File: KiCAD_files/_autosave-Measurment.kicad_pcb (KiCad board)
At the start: 2 copper layers, 90 x 63 mm, 66 parts, among them J1 Measurment_stage_outline_outp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, J2 Measurment_stage_outline_sign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, J3 Conn_01x02, U1 NMA1505SC, U2 AMC1100, U3 AMC1100, U4 AMC1311, U5 R-78C5.0-1.0, U6 AMS1117-3.3, U7 NMA1505SC

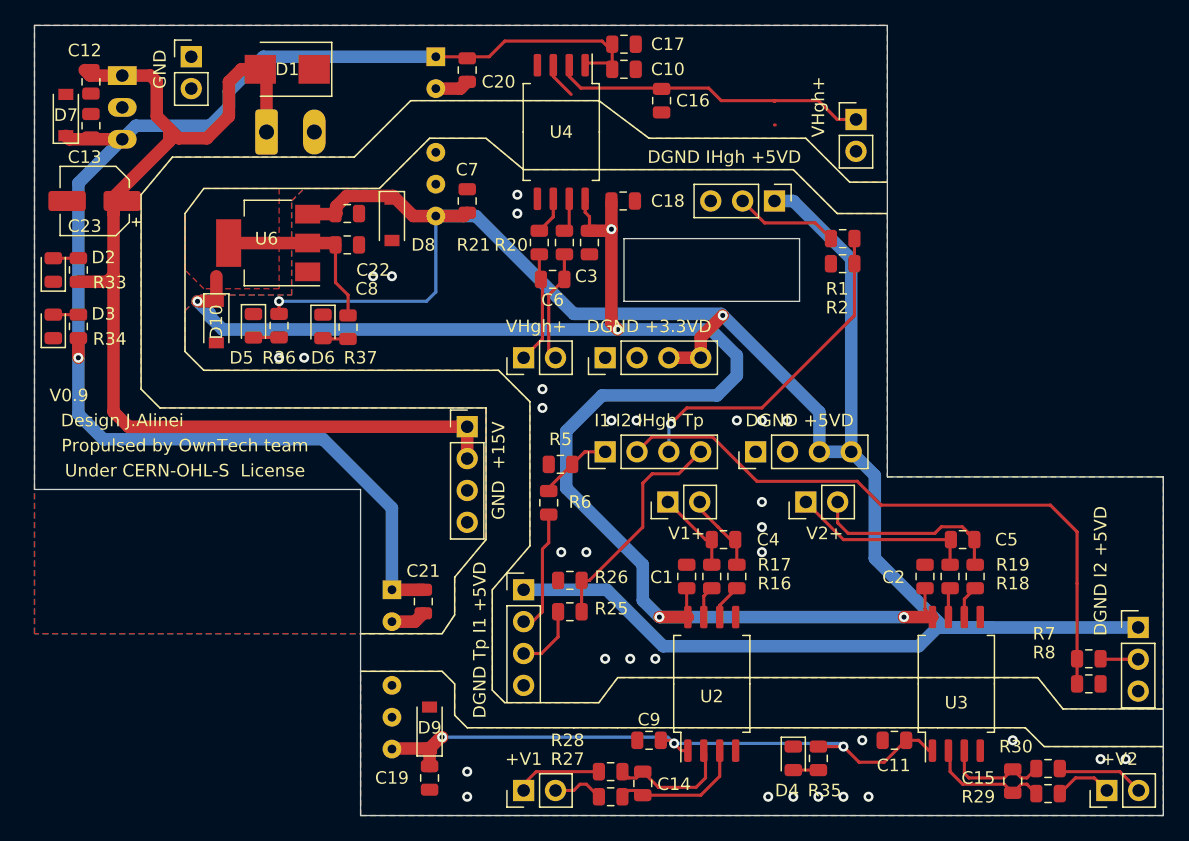
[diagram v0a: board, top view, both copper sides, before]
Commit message: Changed all the headers to improve mezzanine height
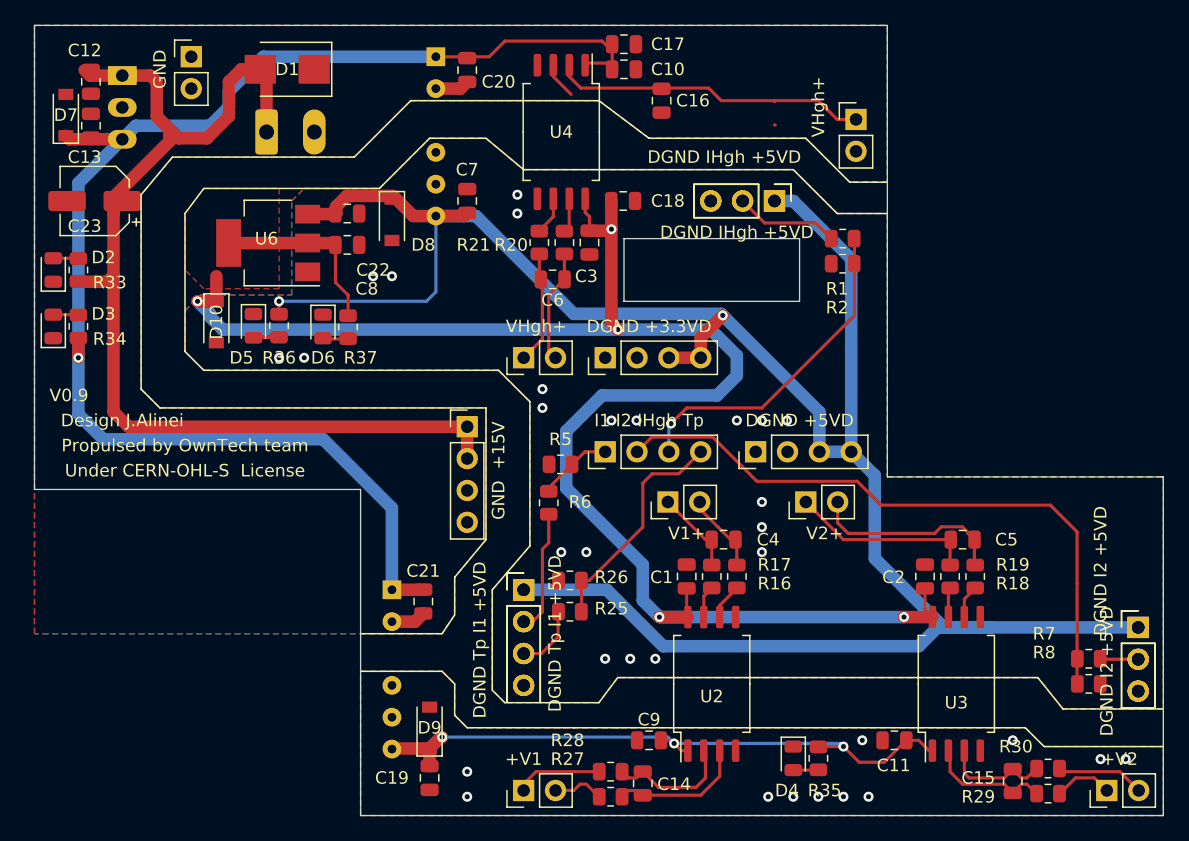
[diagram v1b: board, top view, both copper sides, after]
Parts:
- J1: value Measurment_stage_outline_outputs -> Board outline
